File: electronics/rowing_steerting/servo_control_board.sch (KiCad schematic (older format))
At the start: 20 parts, among them J1 Conn_01x02_Male, J10 Conn_01x03_Female, J11 Conn_01x03_Female, J2 Conn_01x02_Male, J3 Conn_01x02_Male, J4 Conn_01x02_Male, J5 Conn_01x02_Male, J6 Conn_01x03_Female, J7 Conn_01x03_Female, J8 Conn_01x03_Female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

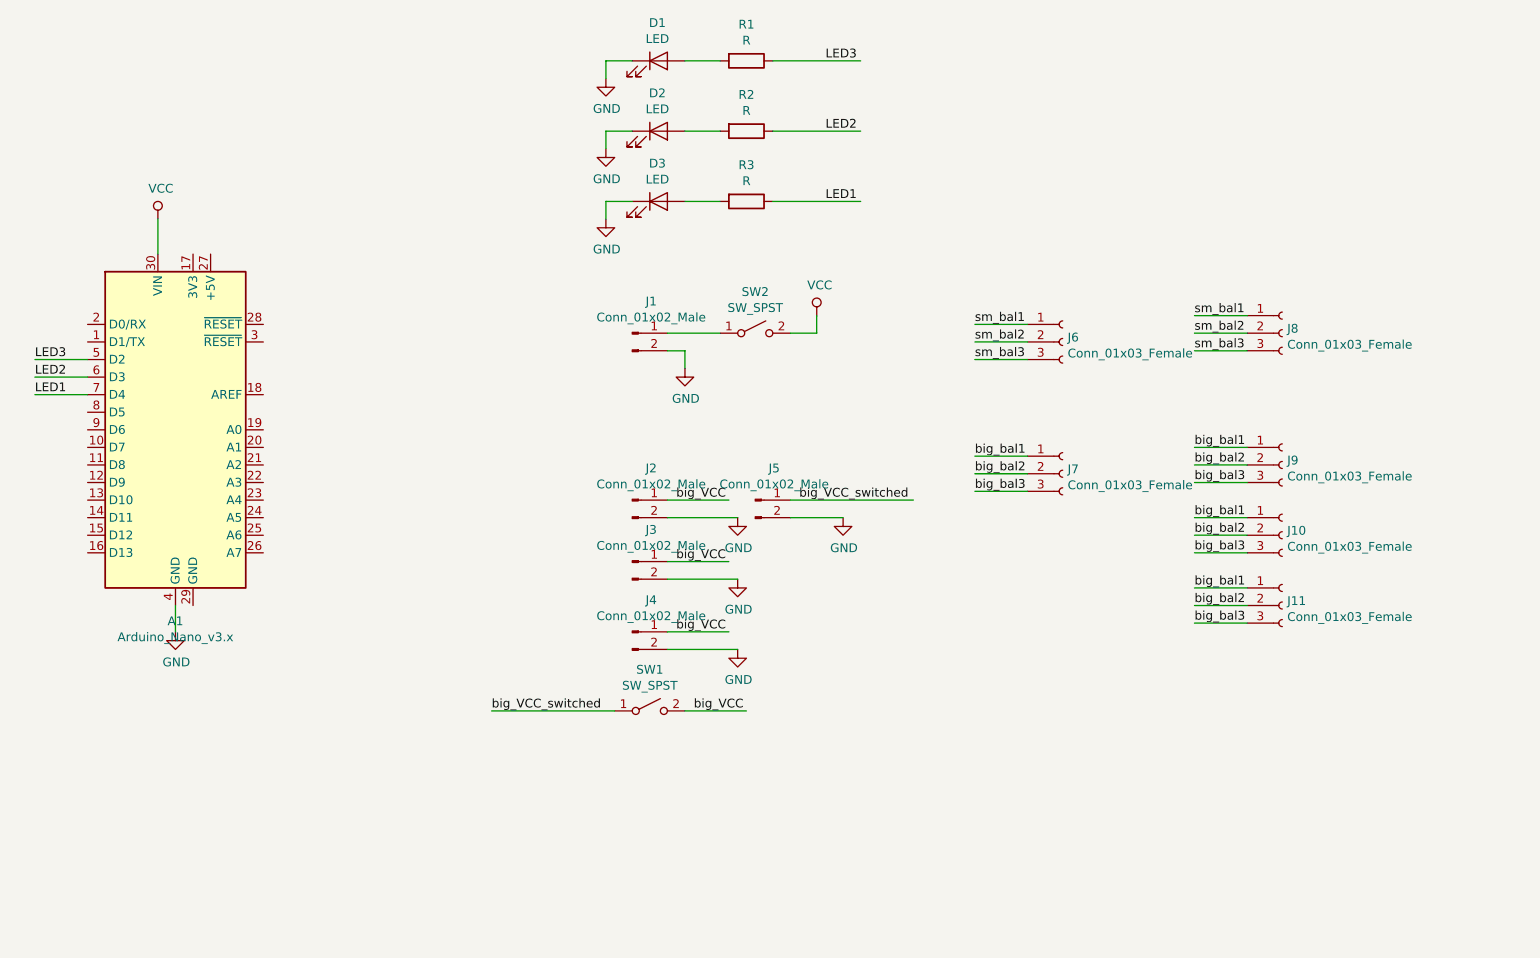
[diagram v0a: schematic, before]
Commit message: update schematic
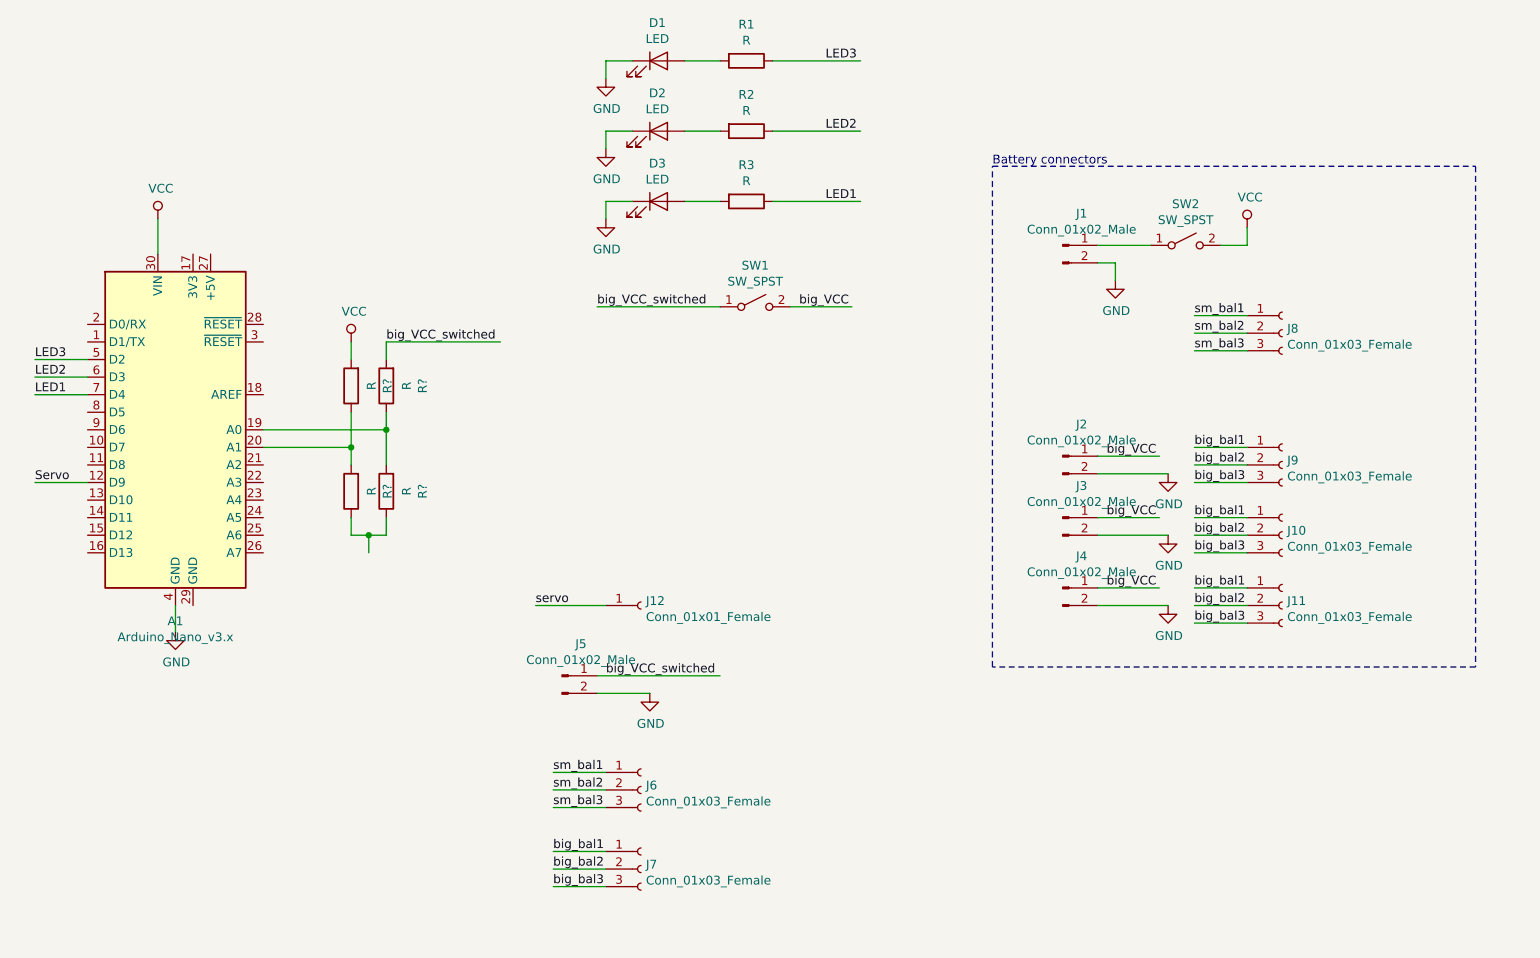
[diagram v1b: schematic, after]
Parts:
- added J12: Conn_01x01_Female, Connector_PinSocket_2.54mm:PinSocket_1x01_P2.54mm_Vertical, symbol Connector:Conn_01x01_Female
- added R? (x4): R, Resistor_SMD:R_1206_3216Metric_Pad1.42x1.75mm_HandSolder, symbol Device:R
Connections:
- net labels added: Servo, servo
- wire segments 50 -> 66
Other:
- note added: "Battery connectors"
- moved on the sheet: J1, J2, J3, J4, J5, J6, J7, SW1, SW2

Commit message: added gerbers rowing_steering board
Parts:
- A1: symbol MCU_Module:Arduino_Nano_v3.x -> servo_control_board-rescue:Arduino_Nano_v3.x-MCU_Module
- gave numbers to parts that had none: 4
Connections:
- net labels removed: Servo
- wire segments 66 -> 68
- no-connect marks 0 -> 21
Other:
- moved on the sheet: J10, J11, J12, J2, J3, J4, J5, J6, J7, J8, J9

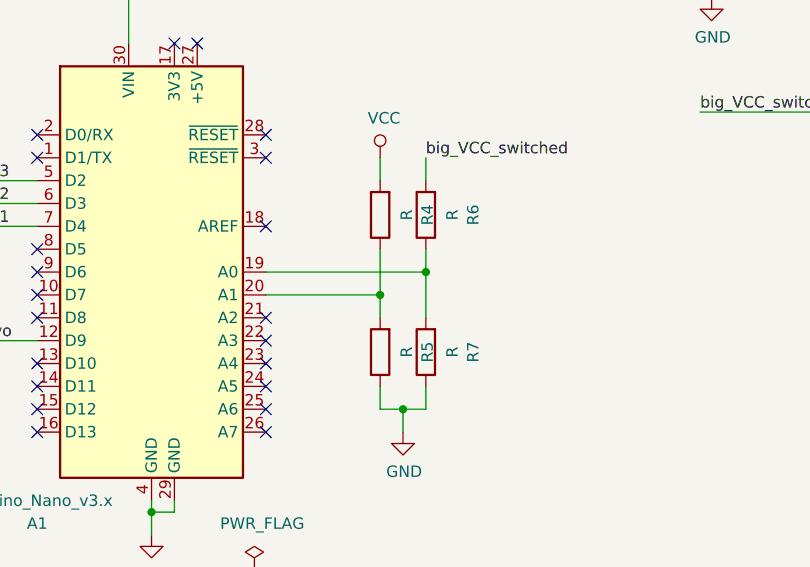
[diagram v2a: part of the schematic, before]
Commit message: Added buttons board
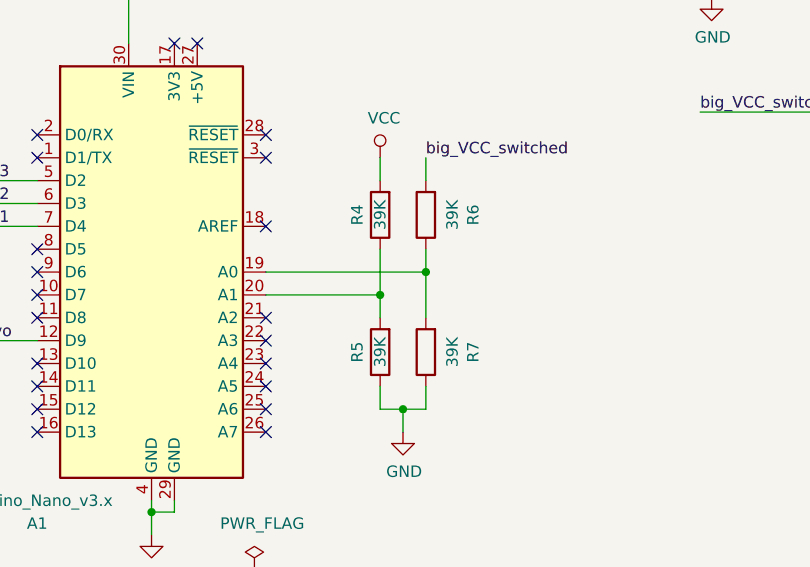
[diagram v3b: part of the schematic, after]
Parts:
- R4, R5, R6, R7: value R -> 39K
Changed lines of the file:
@@
 EESchema Schematic File Version 4
-LIBS:servo_control_board-cache
-EELAYER 29 0
+EELAYER 30 0
 EELAYER END
 $Descr A4 11693 8268
@@
 Wire Wire Line
 	6050 1350 6250 1350
-Wire Wire Line
-	6550 1350 7050 1350
-Text Label 7050 1350 0    50   ~ 0
-LED2
 $Comp
 L power:GND #PWR0110
@@
 U 1 1 5E2A01F0
 P 4150 3400
-F 0 "R5" V 3943 3400 50  0000 C CNN
-F 1 "R" V 4034 3400 50  0000 C CNN
+F 0 "R5" V 4250 3400 50  0000 C CNN
+F 1 "39K" V 4150 3400 50  0000 C CNN
 F 2 "Resistor_SMD:R_1206_3216Metric_Pad1.42x1.75mm_HandSolder" V 4080 3400 50  0001 C CNN
 F 3 "~" H 4150 3400 50  0001 C CNN
@@
 P 4350 3400
 F 0 "R7" V 4143 3400 50  0000 C CNN
-F 1 "R" V 4234 3400 50  0000 C CNN
+F 1 "39K" V 4234 3400 50  0000 C CNN
 F 2 "Resistor_SMD:R_1206_3216Metric_Pad1.42x1.75mm_HandSolder" V 4280 3400 50  0001 C CNN
 F 3 "~" H 4350 3400 50  0001 C CNN
@@
 P 4350 2800
 F 0 "R6" V 4143 2800 50  0000 C CNN
-F 1 "R" V 4234 2800 50  0000 C CNN
+F 1 "39K" V 4234 2800 50  0000 C CNN
 F 2 "Resistor_SMD:R_1206_3216Metric_Pad1.42x1.75mm_HandSolder" V 4280 2800 50  0001 C CNN
 F 3 "~" H 4350 2800 50  0001 C CNN
@@
 U 1 1 5E2A14A0
 P 4150 2800
-F 0 "R4" V 3943 2800 50  0000 C CNN
-F 1 "R" V 4034 2800 50  0000 C CNN
+F 0 "R4" V 4250 2800 50  0000 C CNN
+F 1 "39K" V 4150 2800 50  0000 C CNN
 F 2 "Resistor_SMD:R_1206_3216Metric_Pad1.42x1.75mm_HandSolder" V 4080 2800 50  0001 C CNN
 F 3 "~" H 4150 2800 50  0001 C CNN
@@
 	1    0    0    -1
 $EndComp
+Text Label 7050 1350 0    50   ~ 0
+LED2
+Wire Wire Line
+	6550 1350 7050 1350
 $EndSCHEMATC
